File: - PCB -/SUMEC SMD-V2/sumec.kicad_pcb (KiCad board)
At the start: 2 copper layers, 90 x 55 mm, 55 parts, among them IC1 XT30U-F, IC2 DRV8874PWPR, IC3 DRV8874PWPR, J1 Conn_01x04_Pin, J10 Conn_01x03_Pin, J2 Conn_01x01_Pin, J3 Conn_01x04_Pin, J4 Conn_01x04_Pin, J5 TYPE-C-31-M-12, J6 Conn_01x06_Pin, J7 Conn_01x06_Pin, J8 Conn_01x06_Pin, J9 Conn_01x03_Pin, SW1 SW_Push, SW2 SW_Push, SW3 SW_Push, SW4 SW_DPDT_x2, U2 ESP32-S3-WROOM-1, U3 USBLC6-2SC6, U5 TSOP382xx, U6 LM1084IS-5.0/NOPB, U7 LM1084IS-3.3/NOPB

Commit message: schematic miniupdate
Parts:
- removed C16: 10uF.hb, Capacitor_SMD:CP_Elec_4x5.8
- removed C17: 100nF.hb, Capacitor_SMD:C_0805_2012Metric_Pad1.18x1.45mm_HandSolder
- removed U6: LM1084IS-5.0/NOPB, Package_TO_SOT_SMD:TO-263-3_TabPin4
- removed U7: LM1084IS-3.3/NOPB, Package_TO_SOT_SMD:TO-263-3_TabPin4
- added U1: LM1084-3.3, Package_TO_SOT_SMD:TO-263-3_TabPin2, F.Cu at (106.7, 74.6)
- added U4: LM1084-5.0, Package_TO_SOT_SMD:TO-263-3_TabPin2, F.Cu at (119.1, 74.6)
- moved J9 229.7 mm to (42.4, 56.1), turned to 90 degrees
- moved J10 223.2 mm to (50.2, 56.1), turned to 90 degrees
- moved C11 221.8 mm to (61.6, 130.3), turned to 90 degrees
- moved J3 221.1 mm to (57.5, 53.1), turned to 90 degrees
- moved R1 220.6 mm to (54.4, 166.3), turned to 90 degrees
- moved R3 216.6 mm to (57.3, 166.3), turned to 90 degrees
- moved J4 216.1 mm to (64.5, 53.1), turned to 90 degrees
- moved C12 214.5 mm to (67.5, 130.3), turned to 90 degrees
- moved R4 212.6 mm to (60.2, 166.3), turned to 90 degrees
- moved C1 209.9 mm to (54.4, 161.5), turned to 90 degrees
- moved C8 209.0 mm to (57.4, 156.7), turned to 90 degrees
- moved R5 208.5 mm to (63.2, 166.3), turned to 90 degrees
- moved C13 207.2 mm to (73.3, 130.3), turned to 90 degrees
- moved C2 205.8 mm to (57.4, 161.5), turned to 90 degrees
- moved C9 204.9 mm to (60.4, 156.7), turned to 90 degrees
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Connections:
- C10 pad 1: VM -> +12V
- C19 pad 1: VM -> +12V
- C2 pad 1: VM -> Net-(IC3-VM)
- C5 pad 1: VM -> +12V
- C6 pad 2: VM -> +12V
- IC2 pad 11: VM -> +12V
- IC3 pad 11: VM -> Net-(IC3-VM)
- SW4 pad 1: VM -> +12V

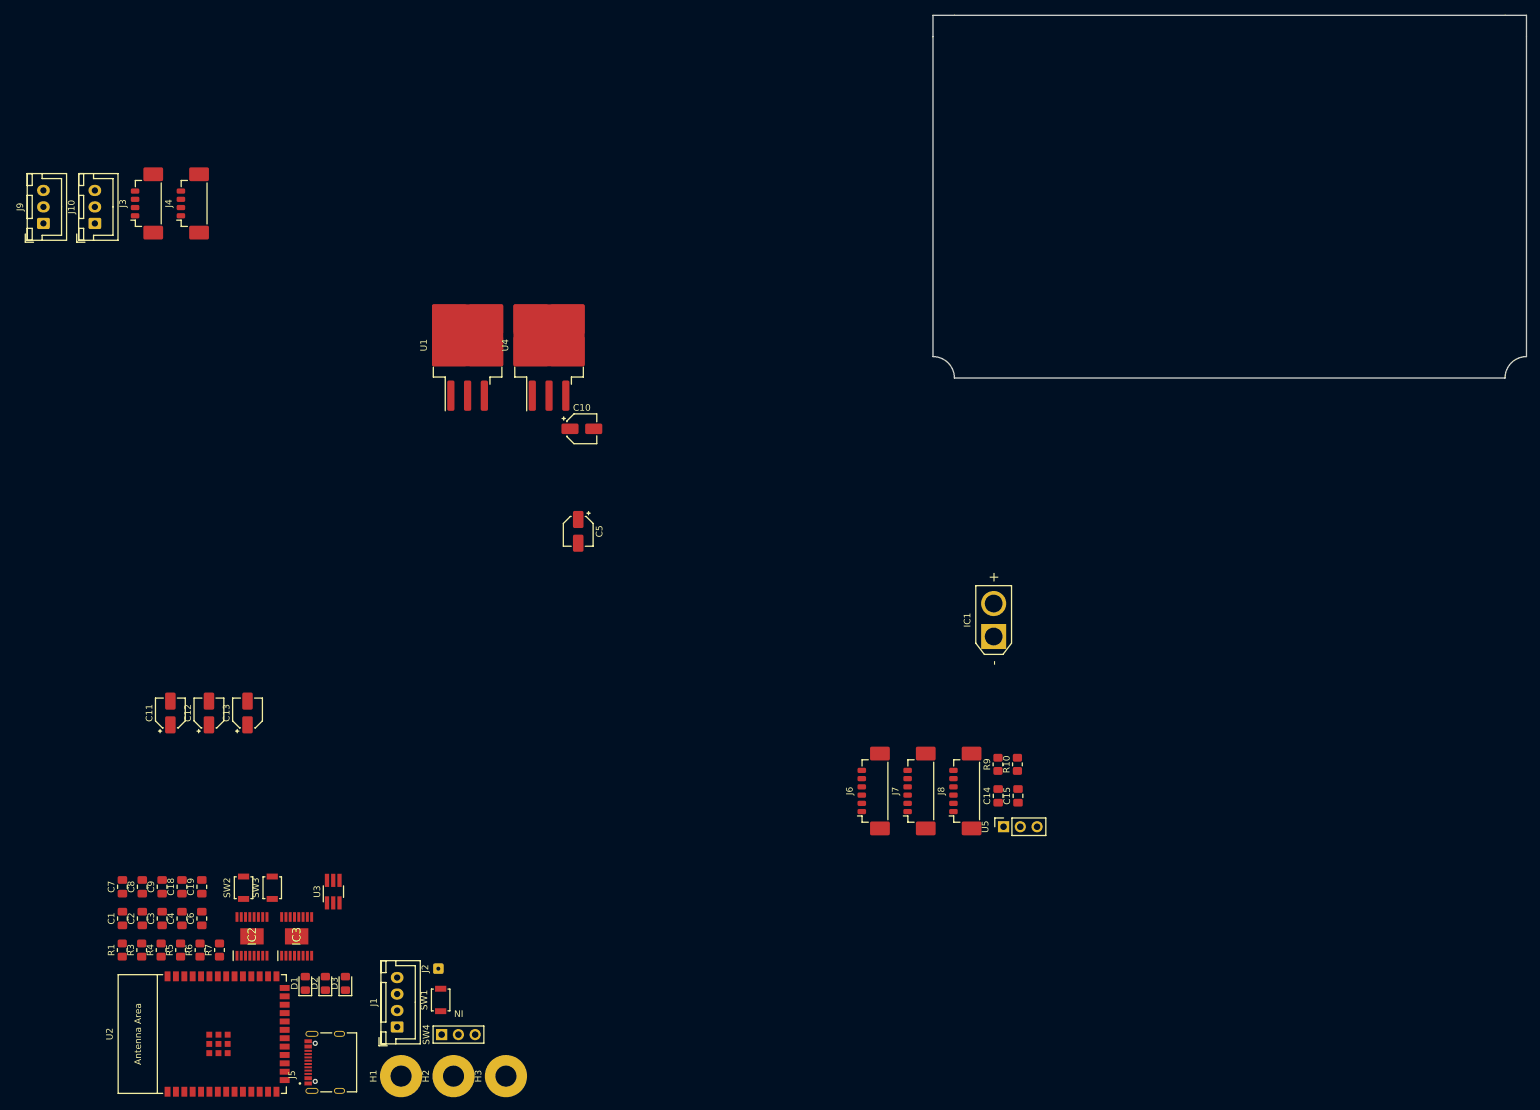
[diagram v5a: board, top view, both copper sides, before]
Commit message: New switch
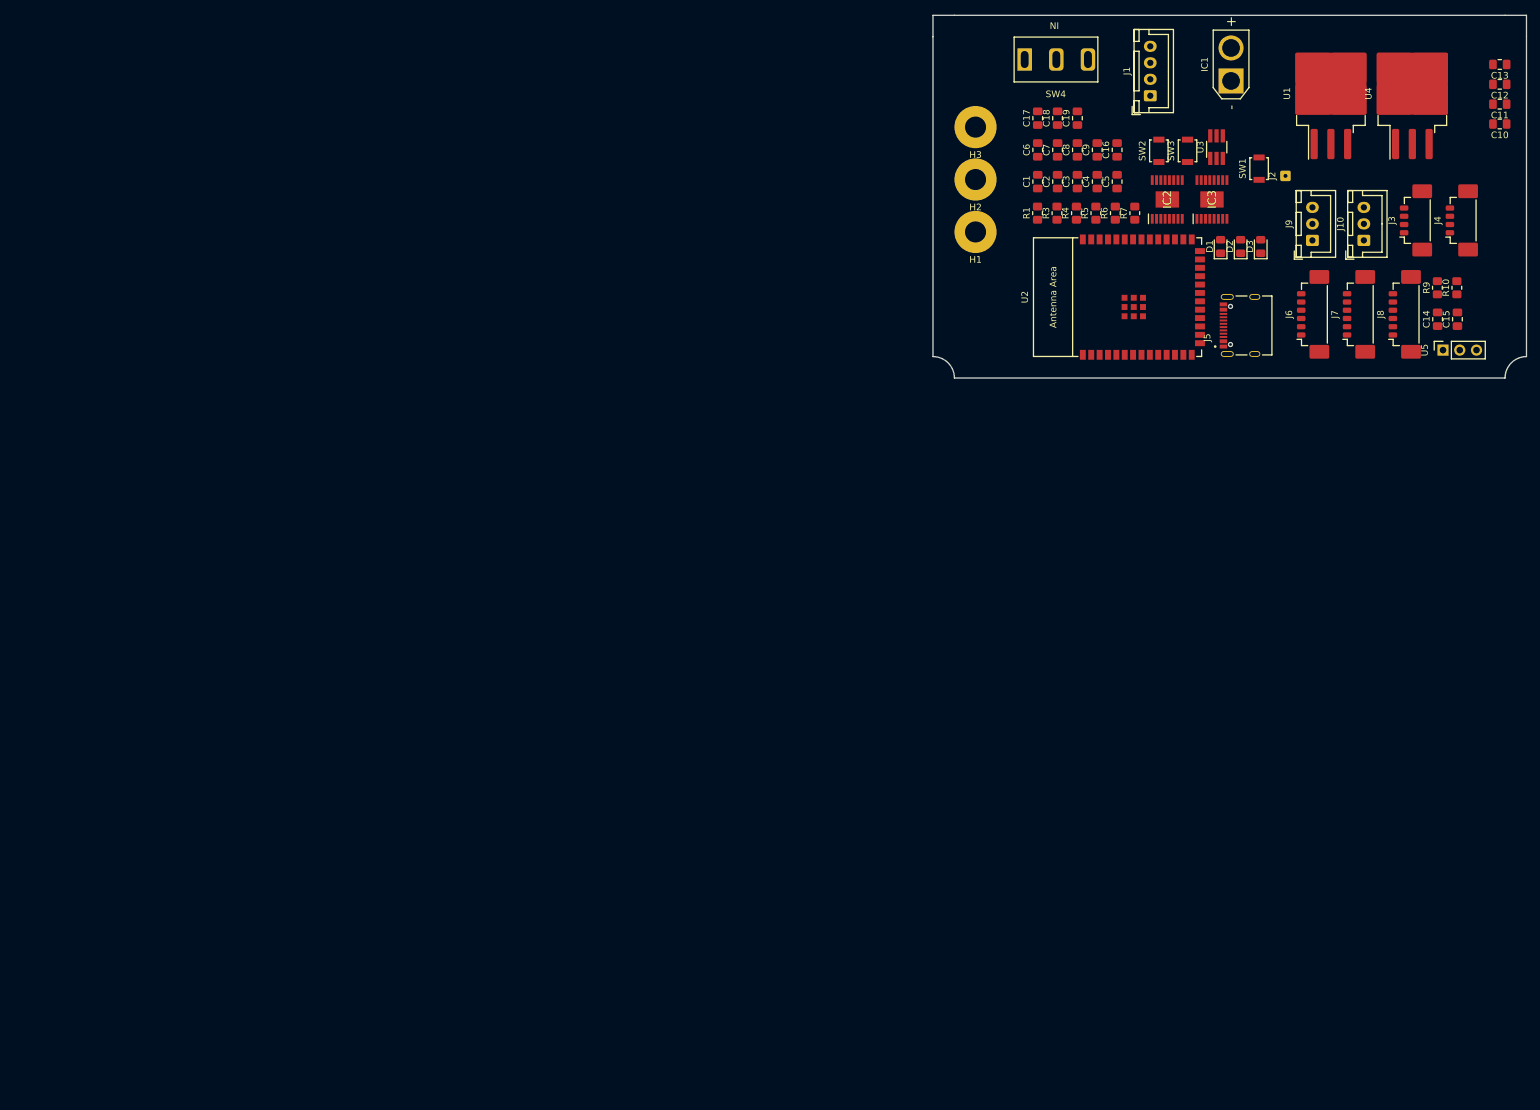
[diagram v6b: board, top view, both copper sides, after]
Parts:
- added C16: 10uF.hb, Capacitor_SMD:C_0805_2012Metric_Pad1.18x1.45mm_HandSolder, F.Cu at (205.2, 45.0)
- added C17: 100nF.hb, Capacitor_SMD:C_0805_2012Metric_Pad1.18x1.45mm_HandSolder, F.Cu at (193.2, 40.1)
- C10, C11, C12, C13, C5: footprint Capacitor_SMD:CP_Elec_4x5.8 -> Capacitor_SMD:C_0805_2012Metric_Pad1.18x1.45mm_HandSolder
- SW4: footprint sumec-smdV2_library:Custom_SPDT_Switch -> sumec-smdV2_library:Custom_SPDT_4.8mm_Switch
- moved C11 221.7 mm to (263.2, 38.0), turned to 180 degrees
- moved C12 217.7 mm to (263.2, 35.0), turned to 180 degrees
- moved C13 213.9 mm to (263.2, 32.0), turned to 180 degrees
- moved J10 192.5 mm to (242.6, 58.7)
- moved J3 192.5 mm to (250.0, 55.6)
- moved J4 192.5 mm to (256.9, 55.6)
- moved J9 192.5 mm to (234.8, 58.7)
- moved J1 181.6 mm to (210.2, 36.8)
- moved C7 180.5 mm to (196.2, 45.0)
- moved C8 180.5 mm to (199.2, 45.0)
- moved C9 180.5 mm to (202.2, 45.0)
- moved C1 178.2 mm to (193.2, 49.8)
- moved C2 178.2 mm to (196.2, 49.8)
- moved C4 178.2 mm to (202.2, 49.8)
- moved D1 178.2 mm to (220.9, 59.6)
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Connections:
- C2 pad 1: Net-(IC3-VM) -> +12V
- IC3 pad 11: Net-(IC3-VM) -> +12V

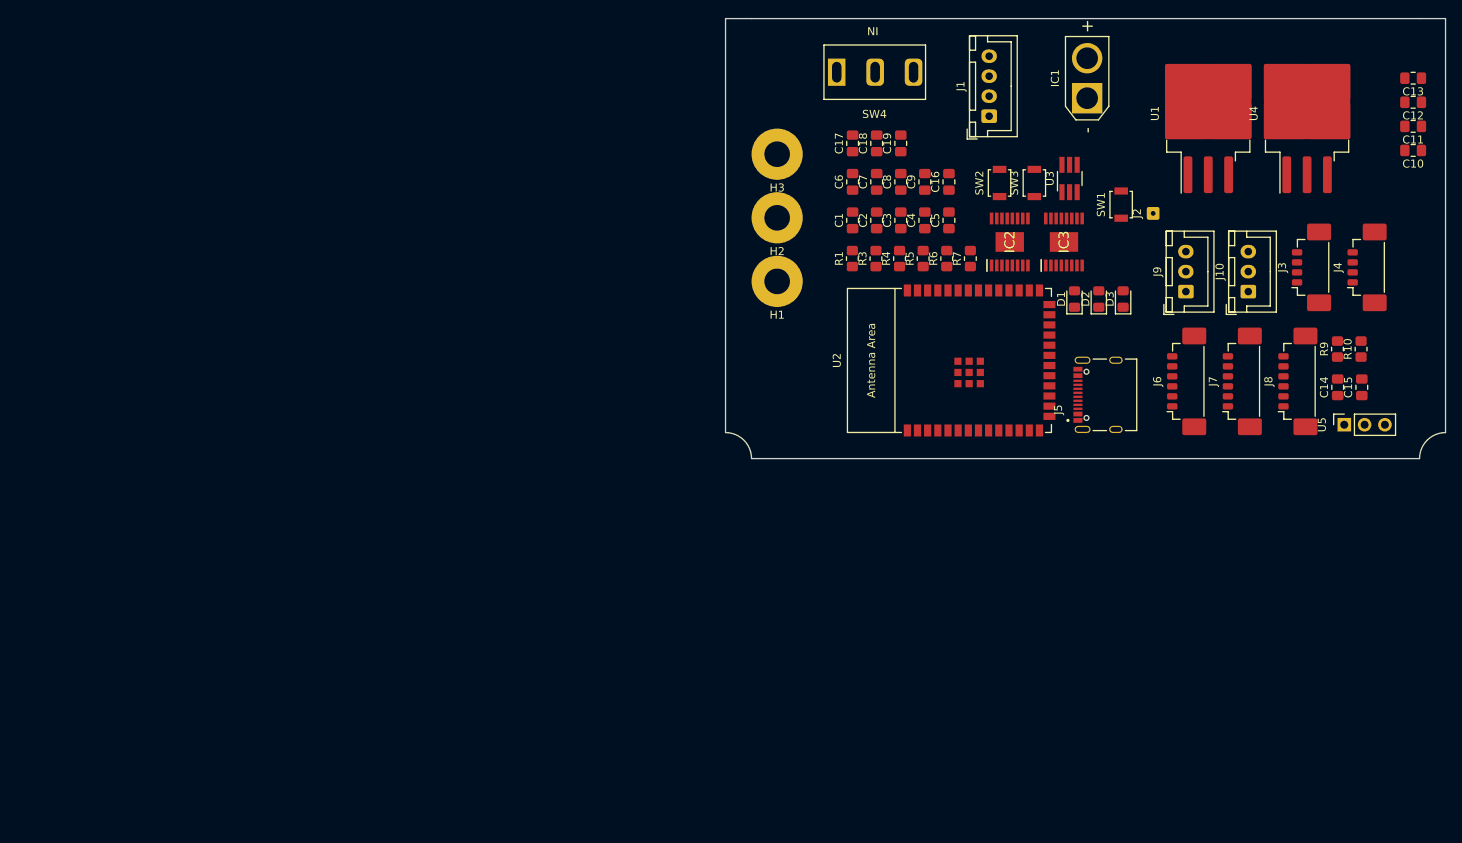
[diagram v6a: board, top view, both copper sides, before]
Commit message: 3d components models, footprint updates
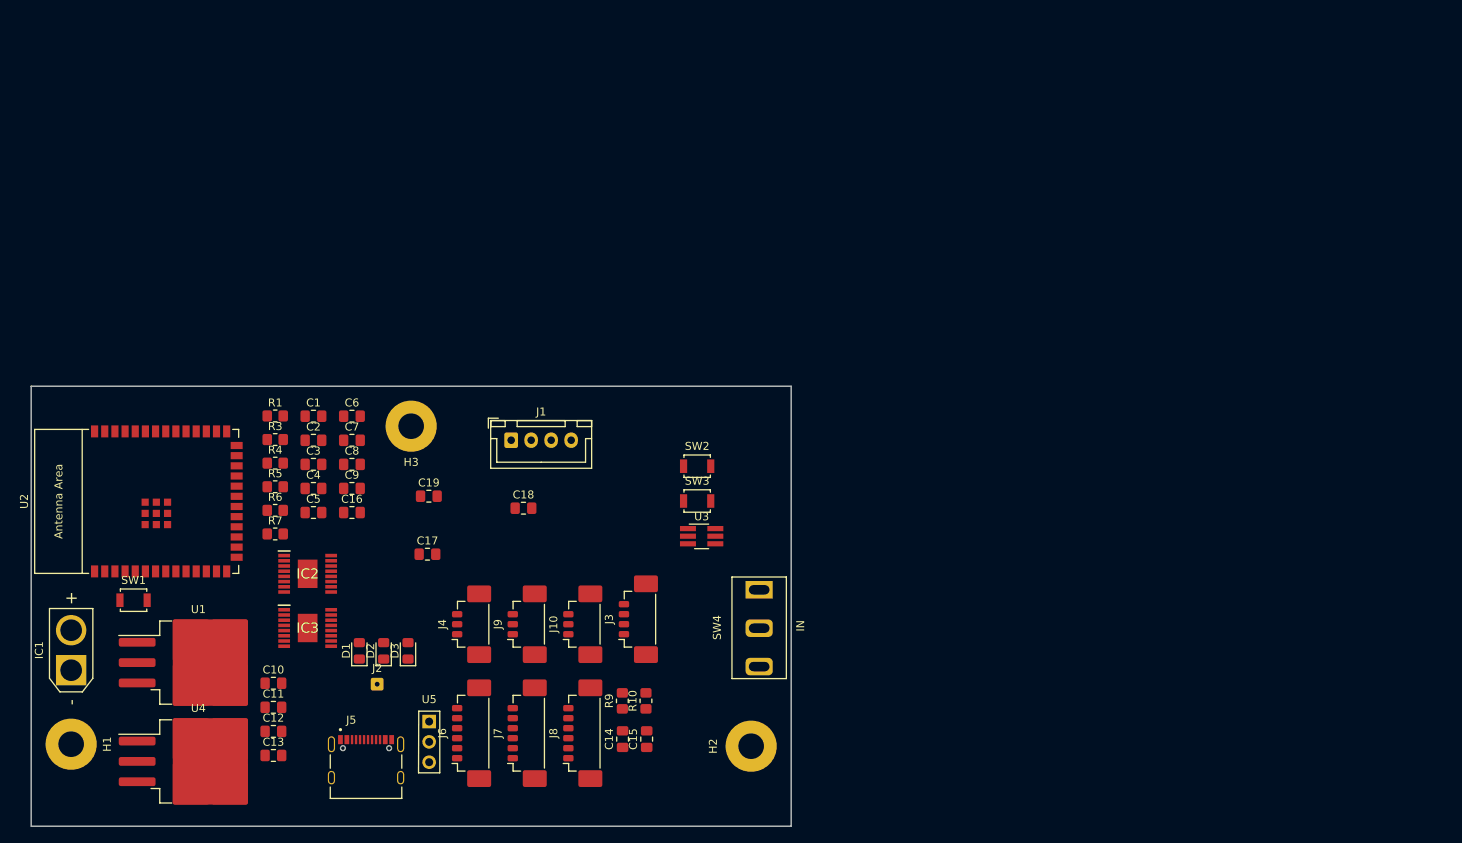
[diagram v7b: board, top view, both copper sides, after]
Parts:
- J10, J9: footprint Connector_JST:JST_XH_B3B-XH-A_1x03_P2.50mm_Vertical -> Connector_Molex:Molex_PicoBlade_53398-0371_1x03-1MP_P1.25mm_Vertical
- J4: value Conn_01x04_Pin -> Conn_01x03_Pin; footprint Connector_Molex:Molex_PicoBlade_53398-0471_1x04-1MP_P1.25mm_Vertical -> Connector_Molex:Molex_PicoBlade_53398-0371_1x03-1MP_P1.25mm_Vertical
- U5: footprint Connector_PinSocket_2.54mm:PinSocket_1x03_P2.54mm_Vertical -> sumec-smdV2_library:TSOP
- moved C13 165.7 mm to (120.8, 116.7), turned to 0 degrees
- moved C12 162.7 mm to (120.8, 113.7), turned to 0 degrees
- moved U4 160.5 mm to (111.4, 117.4), turned to 0 degrees
- moved C11 159.9 mm to (120.8, 110.6), turned to 0 degrees
- moved C10 157.3 mm to (120.8, 107.6), turned to 0 degrees
- moved IC1 145.7 mm to (95.5, 106.0)
- moved U1 143.7 mm to (111.4, 105.0), turned to 0 degrees
- moved SW1 133.0 mm to (103.3, 97.2), turned to 0 degrees
- moved J4 120.5 mm to (145.0, 100.3)
- moved U5 120.3 mm to (140.2, 112.4), turned to 0 degrees
- moved J2 113.5 mm to (133.8, 107.8), turned to 0 degrees
- moved IC3 106.1 mm to (125.1, 100.7), turned to 0 degrees
- moved H1 105.5 mm to (95.5, 115.2), turned to 0 degrees
- moved J5 105.2 mm to (132.4, 119.4), turned to 0 degrees
- moved U2 103.1 mm to (106.7, 84.9)
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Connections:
- J10 pad 1: SHARP 1 -> SHARP 2
- J9 pad 1: SHARP 2 -> SHARP 1
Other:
- board size 90 x 55 mm -> 95 x 55 mm

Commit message: Borard upd
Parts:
- removed R3: 220, Resistor_SMD:R_0805_2012Metric_Pad1.20x1.40mm_HandSolder
- added R2: 220, Resistor_SMD:R_0805_2012Metric_Pad1.20x1.40mm_HandSolder, F.Cu at (106.2, 97.0)
- C10, C11, C12, C13, C16, C5: footprint Capacitor_SMD:C_0805_2012Metric_Pad1.18x1.45mm_HandSolder -> Capacitor_Tantalum_SMD:CP_EIA-2012-12_Kemet-R_Pad1.30x1.05mm_HandSolder
- C14, C15, C3: footprint Capacitor_SMD:C_0805_2012Metric_Pad1.18x1.45mm_HandSolder -> Capacitor_Tantalum_SMD:CP_EIA-2012-12_Kemet-R_Pad1.30x1.05mm_HandSolder; moved to B.Cu
- C19, C4, J1, J10, J3, J4, J9, R10, R4, R9: moved to B.Cu
- C2: value 100nF.hb -> 220nF.hb; moved to B.Cu
- moved SW2 80.2 mm to (95.2, 97.0)
- moved U4 75.9 mm to (176.0, 77.6), turned to 90 degrees
- moved U3 70.9 mm to (105.2, 105.5)
- moved C10 63.7 mm to (180.8, 86.3), turned to -90 degrees
- moved IC1 60.2 mm to (154.2, 119.2), turned to 180 degrees
- moved C12 59.5 mm to (175.0, 89.0), turned to 180 degrees
- moved U1 55.8 mm to (160.0, 77.7), turned to 90 degrees
- moved SW3 54.5 mm to (120.2, 74.3), turned to -90 degrees
- moved C14 50.6 mm to (114.8, 104.8)
- moved C11 50.3 mm to (164.8, 86.3), turned to -90 degrees
- moved U5 50.0 mm to (109.8, 72.8), turned to 90 degrees
- moved J8 48.8 mm to (110.5, 119.8), turned to 180 degrees
- moved C13 47.2 mm to (159.0, 89.0), turned to 180 degrees
- moved J5 42.0 mm to (92.6, 105.9), turned to -90 degrees
- moved J9 41.1 mm to (111.2, 105.8)
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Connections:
- C14 pad 1: GND -> +3V3
- C14 pad 2: +3V3 -> GND
- C15 pad 1: GND -> +3V3
- C15 pad 2: +3V3 -> GND
- R1 pad 1: Net-(D2-K) -> Net-(D1-K)
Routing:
- net SCL: track 0.00 -> 93.1 mm
- net SDA: track 0.00 -> 90.9 mm
- net GND: track 0.00 -> 19.0 mm, vias 0 -> 4
- added copper zone on B.Cu, net GND
- added copper zone on F.Cu, net GND
